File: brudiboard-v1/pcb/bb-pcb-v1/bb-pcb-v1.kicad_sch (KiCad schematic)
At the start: 204 parts, among them U1 Raspberry_Pi_Pico

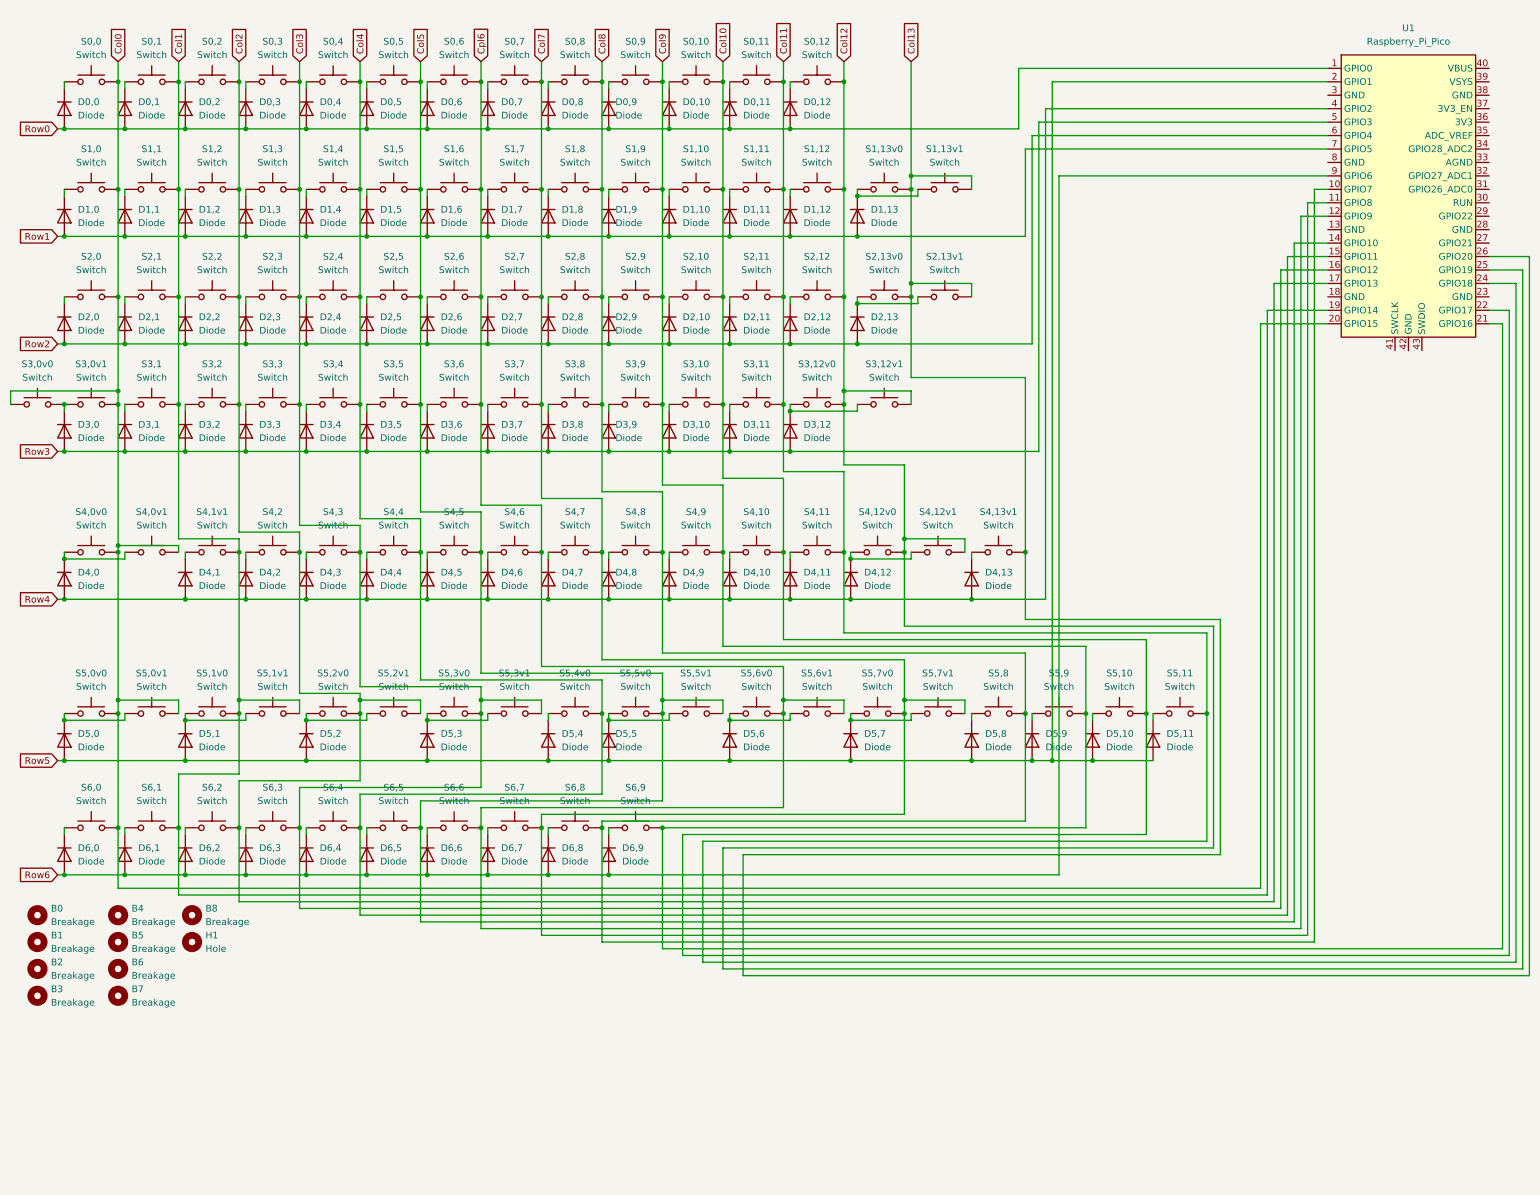
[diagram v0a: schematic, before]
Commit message: brudiboard-v1 pcb v1 finalized and exported
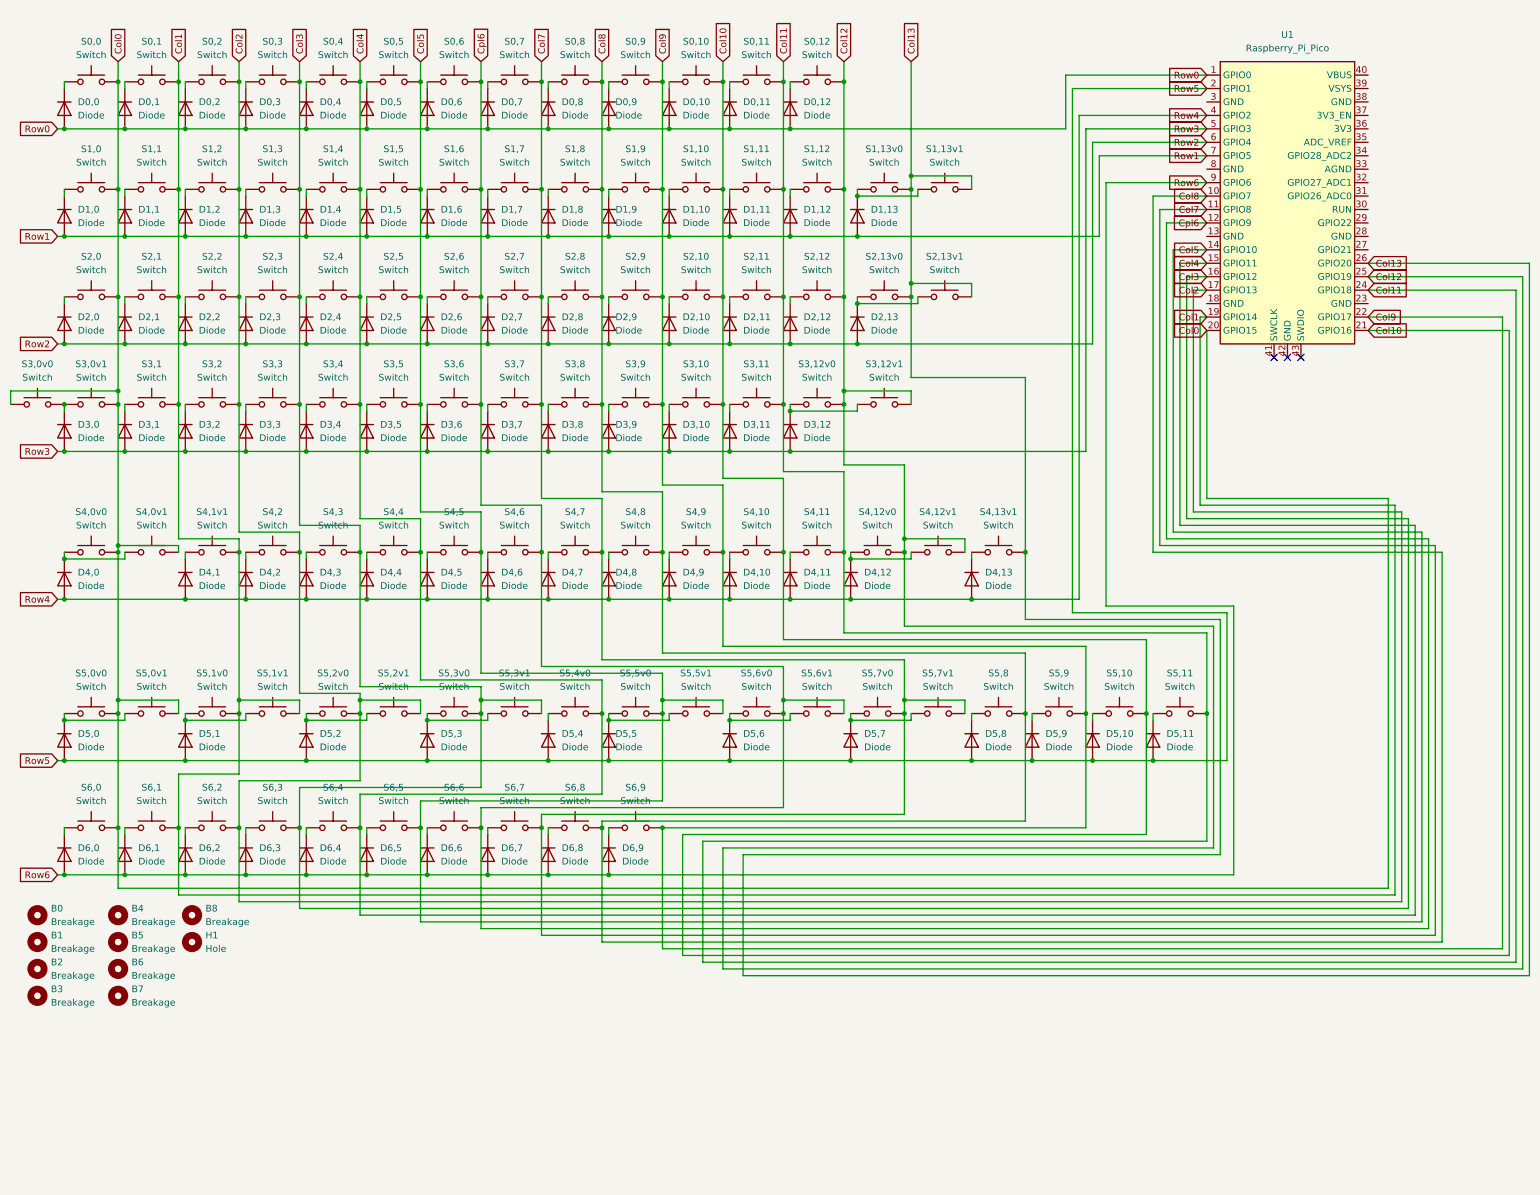
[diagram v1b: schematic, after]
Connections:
- net Col10: now also U1.21 (GPIO16); no longer U1.22 (GPIO17)
- net Col9: now also U1.22 (GPIO17); no longer U1.21 (GPIO16)
- no-connect marks 0 -> 3
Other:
- moved on the sheet: U1

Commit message: brudiboard-v1 case production files + pcb rev 3
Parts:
- removed H1: Hole, ScottoKeebs_Hotswap:cable_hole, symbol ScottoKeebs:Placeholder_Mounting_Hole
- added D5,7, D5,8: Diode, ScottoKeebs_Components:Diode_DO-35, symbol ScottoKeebs:Placeholder_Diode
- added S5,3, S5,5: Switch, ScottoKeebs_Hotswap:Hotswap_MX_3.00u, symbol ScottoKeebs:Placeholder_Switch
- added ST1, ST2, ST3, ST8, ST9: Stabilizer, ScottoKeebs_Stabilizer:Stabilizer_MX_2.00u_Exact, symbol ScottoKeebs:Placeholder_Mounting_Hole
- added ST4: Stabilizer, ScottoKeebs_Stabilizer:Stabilizer_MX_6.25u_Exact, symbol ScottoKeebs:Placeholder_Mounting_Hole
- added ST5: Stabilizer, ScottoKeebs_Stabilizer:Stabilizer_MX_7.00u_Exact, symbol ScottoKeebs:Placeholder_Mounting_Hole
- added ST6: Stabilizer, ScottoKeebs_Stabilizer:Stabilizer_MX_3.00u_Exact_Left, symbol ScottoKeebs:Placeholder_Mounting_Hole
- added ST7: Stabilizer, ScottoKeebs_Stabilizer:Stabilizer_MX_3.00u_Exact_Right, symbol ScottoKeebs:Placeholder_Mounting_Hole
- S1,13v0: footprint ScottoKeebs_Hotswap:Hotswap_MX_2.00u_Stab -> ScottoKeebs_Hotswap:Hotswap_MX_2.00u
- S3,12v0: footprint ScottoKeebs_Hotswap:Hotswap_MX_2.25u_Stab_Inv -> ScottoKeebs_Hotswap:Hotswap_MX_2.25u
- S3,12v1: footprint ScottoKeebs_Hotswap:Hotswap_MX_ISOEnter_Stab -> ScottoKeebs_Hotswap:Hotswap_MX_ISOEnter
- S4,0v0: footprint ScottoKeebs_Hotswap:Hotswap_MX_2.25u_Stab -> ScottoKeebs_Hotswap:Hotswap_MX_2.25u
- S4,12v0: footprint ScottoKeebs_Hotswap:Hotswap_MX_2.75u_Stab_Inv -> ScottoKeebs_Hotswap:Hotswap_MX_2.75u
- S5,4v0: renamed from S5,3v0; footprint ScottoKeebs_Hotswap:Hotswap_MX_6.25u_Stab_Inv -> ScottoKeebs_Hotswap:Hotswap_MX_6.25u
- S5,4v1: renamed from S5,3v1; footprint ScottoKeebs_Hotswap:Hotswap_MX_7.00u_Stab -> ScottoKeebs_Hotswap:Hotswap_MX_7.00u
- renumbered D5,8 to D5,10, D5,9 to D5,11, D5,10 to D5,12, D5,11 to D5,13, D5,7 to D5,9, S5,8 to S5,10, S5,9 to S5,11, S5,10 to S5,12, S5,11 to S5,13, S5,4v0 to S5,6, S5,5v0 to S5,7v0, S5,5v1 to S5,7v1, S5,6v0 to S5,8v0, S5,6v1 to S5,8v1, S5,7v0 to S5,9v0, S5,7v1 to S5,9v1
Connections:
- net Col0: now also U1.1 (GPIO0); no longer U1.20 (GPIO15)
- net Col1: now also U1.2 (GPIO1); no longer U1.19 (GPIO14)
- net Col10: now also S5,10.2, U1.14 (GPIO10); no longer S5,12.2, U1.21 (GPIO16)
- net Col11: now also S5,11.2, U1.15 (GPIO11); no longer S5,13.2, U1.24 (GPIO18)
- net Col12: now also S5,12.2, U1.16 (GPIO12); no longer U1.25 (GPIO19)
- net Col13: now also S5,13.2, U1.17 (GPIO13); no longer U1.26 (GPIO20)
- net Col2: now also U1.4 (GPIO2); no longer U1.17 (GPIO13)
- net Col3: now also U1.5 (GPIO3), S5,3.2; no longer S5,4v0.2, S5,4v1.2, U1.16 (GPIO12)
- net Col4: now also S5,4v0.2, S5,4v1.2, U1.6 (GPIO4); no longer S5,6.2, U1.15 (GPIO11)
- net Col5: now also U1.7 (GPIO5), S5,5.2; no longer S5,7v0.2, S5,7v1.2, U1.14 (GPIO10)
- net Col7: now also S5,7v0.2, S5,7v1.2, U1.10 (GPIO7); no longer S5,9v0.2, S5,9v1.2, U1.11 (GPIO8)
- net Col8: now also S5,8v0.2, S5,8v1.2, U1.11 (GPIO8); no longer S5,10.2, U1.10 (GPIO7)
- net Col9: now also S5,9v0.2, S5,9v1.2, U1.12 (GPIO9); no longer S5,11.2, U1.22 (GPIO17)
- net Cpl6: now also S5,6.2, U1.9 (GPIO6); no longer S5,8v0.2, S5,8v1.2, U1.12 (GPIO9)
- net Row0: now also U1.21 (GPIO16); no longer U1.1 (GPIO0)
- net Row1: now also U1.22 (GPIO17); no longer U1.7 (GPIO5)
- net Row2: now also U1.24 (GPIO18); no longer U1.6 (GPIO4)
- net Row3: now also U1.25 (GPIO19); no longer U1.5 (GPIO3)
- net Row4: now also U1.26 (GPIO20); no longer U1.4 (GPIO2)
- net Row5: now also U1.27 (GPIO21), D5,7.2 (A), D5,8.2 (A); no longer U1.2 (GPIO1)
- net Row6: now also U1.29 (GPIO22); no longer U1.9 (GPIO6)
- net at S5,4v0.1, S5,4v1.1: now also D5,4.1 (K); no longer D5,3.1 (K)
- net at S5,7v0.1, S5,7v1.1: now also D5,7.1 (K); no longer D5,5.1 (K)
- net at S5,8v0.1, S5,8v1.1: now also D5,8.1 (K); no longer D5,6.1 (K)
- net at S5,6.1: now also D5,6.1 (K); no longer D5,4.1 (K)
- new net: D5,5.1 (K), S5,5.1
- new net: D5,3.1 (K), S5,3.1
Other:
- moved on the sheet: B0, B1, B2, B3, B4, B5, B6, B7, B8, D5,10, D5,11, D5,12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
